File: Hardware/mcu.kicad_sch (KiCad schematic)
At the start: 10 parts, among them Q1 BSS138DW-7-F, U6 AS7341-DLGT

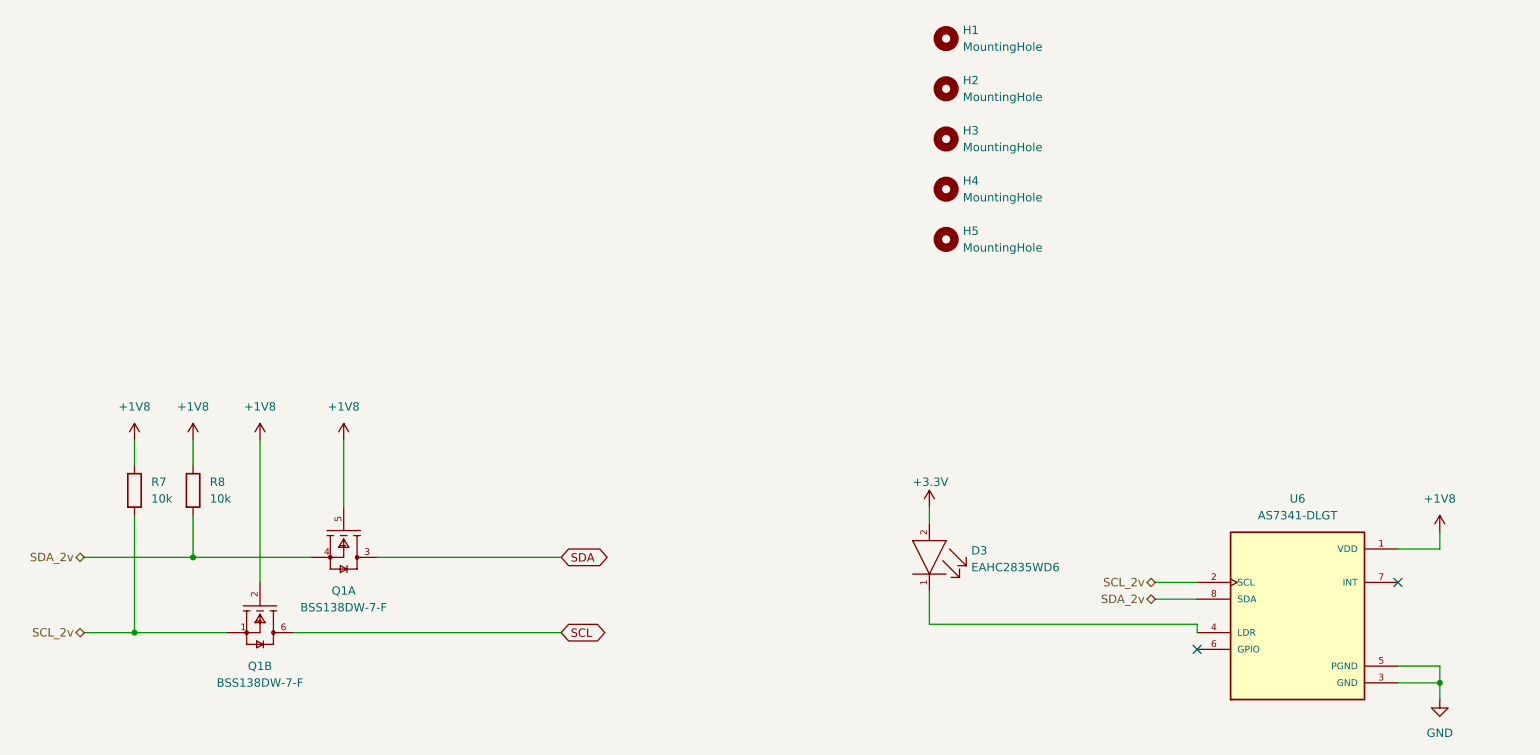
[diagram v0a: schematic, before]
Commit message: Version 0.6 - 4 layer version
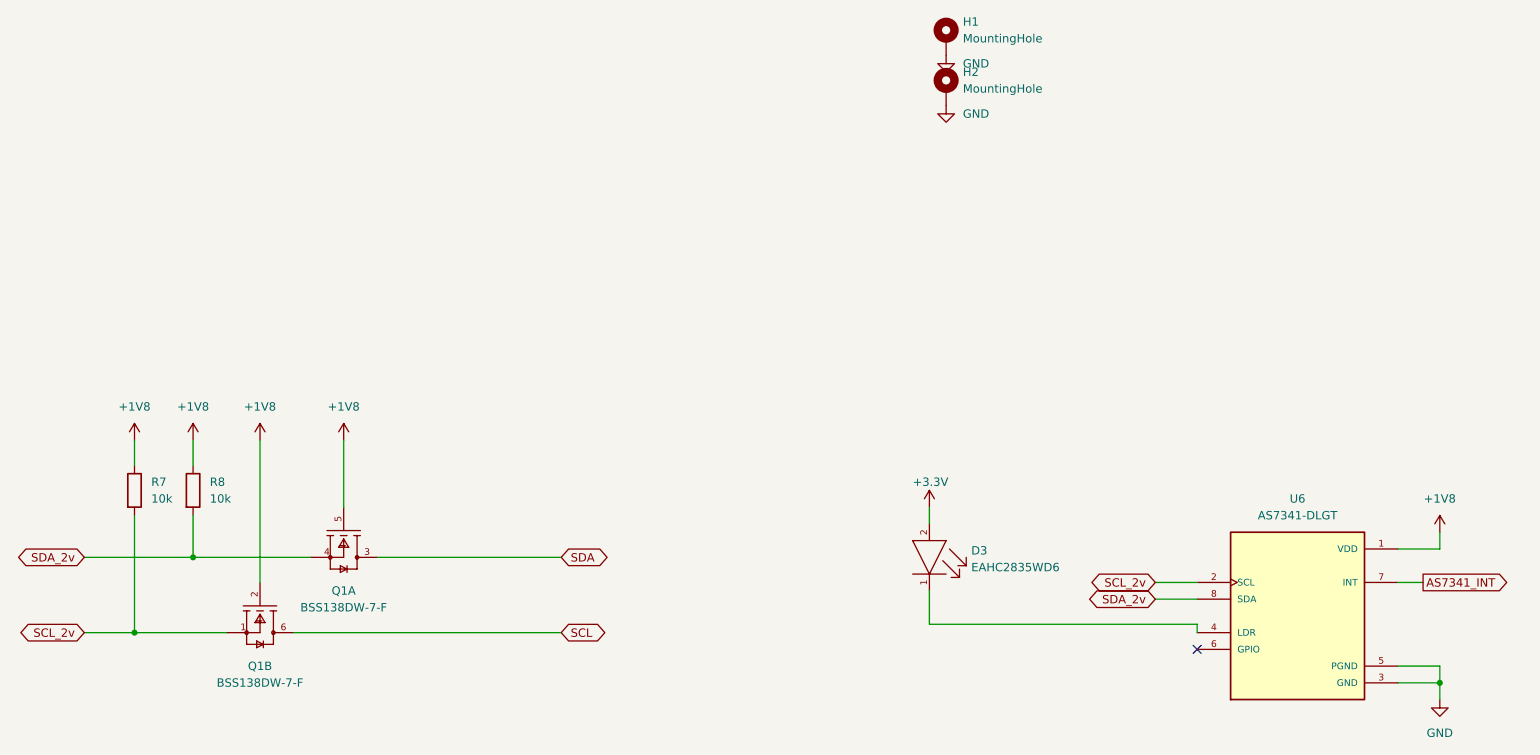
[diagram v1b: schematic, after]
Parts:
- removed H3, H4, H5: MountingHole, MountingHole:MountingHole_2.2mm_M2_ISO7380_Pad, symbol Mechanical:MountingHole
- H1, H2: symbol Mechanical:MountingHole -> Mechanical:MountingHole_Pad
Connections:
- net GND: now also H1.1, H2.1
- net AS7341_INT: now reaches U6.7 (INT)
- no-connect marks 2 -> 1
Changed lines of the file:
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@@
   (junction (at 68.58 110.49) (diameter 0) (color 0 0 0 0)
   )
-  (no_connect (at 251.46 114.3))
   (no_connect (at 220.98 124.46))
   (wire (pts (xy 180.34 102.87) (xy 180.34 105.41))
@@
     (stroke (width 0) (type default) (color 0 0 0 0))
   )
+  (wire (pts (xy 251.46 114.3) (xy 255.27 114.3))
+    (stroke (width 0) (type default) (color 0 0 0 0))
+  )
   (wire (pts (xy 68.58 104.14) (xy 68.58 110.49))
     (stroke (width 0) (type default) (color 0 0 0 0))
@@
   (wire (pts (xy 59.69 121.92) (xy 73.66 121.92))
     (stroke (width 0) (type default) (color 0 0 0 0))
+  )
+  (global_label "SCL_2v" (shape bidirectional) (at 52.07 121.92 180) (fields_autoplaced)
+    (effects (font (size 1.27 1.27)) (justify right))
+    (property "Intersheet References" "${INTERSHEET_REFS}" (id 0) (at 43.0045 121.8406 0)
+      (effects (font (size 1.27 1.27)) (justify right) hide)
+    )
+  )
+  (global_label "SDA_2v" (shape bidirectional) (at 214.63 116.84 180) (fields_autoplaced)
+    (effects (font (size 1.27 1.27)) (justify right))
+    (property "Intersheet References" "${INTERSHEET_REFS}" (id 0) (at 205.504 116.7606 0)
+      (effects (font (size 1.27 1.27)) (justify right) hide)
+    )
   )
   (global_label "SDA" (shape bidirectional) (at 124.46 110.49 0) (fields_autoplaced)
@@
     )
   )
+  (global_label "SDA_2v" (shape bidirectional) (at 52.07 110.49 180) (fields_autoplaced)
+    (effects (font (size 1.27 1.27)) (justify right))
+    (property "Intersheet References" "${INTERSHEET_REFS}" (id 0) (at 42.944 110.4106 0)
+      (effects (font (size 1.27 1.27)) (justify right) hide)
+    )
+  )
+  (global_label "SCL_2v" (shape bidirectional) (at 214.63 114.3 180) (fields_autoplaced)
+    (effects (font (size 1.27 1.27)) (justify right))
+    (property "Intersheet References" "${INTERSHEET_REFS}" (id 0) (at 205.5645 114.2206 0)
+      (effects (font (size 1.27 1.27)) (justify right) hide)
+    )
+  )
+  (global_label "AS7341_INT" (shape output) (at 255.27 114.3 0) (fields_autoplaced)
+    (effects (font (size 1.27 1.27)) (justify left))
+    (property "Intersheet References" "${INTERSHEET_REFS}" (id 0) (at 268.6898 114.2206 0)
+      (effects (font (size 1.27 1.27)) (justify left) hide)
+    )
+  )
   (global_label "SCL" (shape bidirectional) (at 124.46 121.92 0) (fields_autoplaced)
     (effects (font (size 1.27 1.27)) (justify left))
@@
     )
   )
-  (hierarchical_label "SCL_2v" (shape bidirectional) (at 52.07 121.92 180)
-    (effects (font (size 1.27 1.27)) (justify right))
-  )
-  (hierarchical_label "SDA_2v" (shape bidirectional) (at 52.07 110.49 180)
-    (effects (font (size 1.27 1.27)) (justify right))
-  )
-  (hierarchical_label "SDA_2v" (shape bidirectional) (at 214.63 116.84 180)
-    (effects (font (size 1.27 1.27)) (justify right))
-  )
-  (hierarchical_label "SCL_2v" (shape bidirectional) (at 214.63 114.3 180)
-    (effects (font (size 1.27 1.27)) (justify right))
-  )
   (symbol (lib_id "Device:R") (at 68.58 100.33 0) (unit 1)
     (in_bom yes) (on_board yes) (fields_autoplaced)
@@
     (pin "2")
   )
-  (symbol (lib_id "Mechanical:MountingHole") (at 182.88 39.37 0) (unit 1)
-    (in_bom yes) (on_board yes) (fields_autoplaced)
-    (property "Reference" "H2" (id 0) (at 185.42 38.0999 0)
-      (effects (font (size 1.27 1.27)) (justify left))
-    )
-    (property "Value" "MountingHole" (id 1) (at 185.42 40.6399 0)
+  (symbol (lib_id "power:GND") (at 182.88 34.29 0) (unit 1)
+    (in_bom yes) (on_board yes) (fields_autoplaced)
+    (property "Reference" "#PWR0112" (id 0) (at 182.88 40.64 0)
+      (effects (font (size 1.27 1.27)) hide)
+    )
+    (property "Value" "GND" (id 1) (at 185.42 35.5599 0)
+      (effects (font (size 1.27 1.27)) (justify left))
+    )
+    (property "Footprint" "" (id 2) (at 182.88 34.29 0)
+      (effects (font (size 1.27 1.27)) hide)
+    )
+    (property "Datasheet" "" (id 3) (at 182.88 34.29 0)
+      (effects (font (size 1.27 1.27)) hide)
+    )
+    (pin "1")
+  )
+  (symbol (lib_id "Mechanical:MountingHole_Pad") (at 182.88 39.37 0) (unit 1)
+    (in_bom yes) (on_board yes) (fields_autoplaced)
+    (property "Reference" "H2" (id 0) (at 185.42 36.8299 0)
+      (effects (font (size 1.27 1.27)) (justify left))
+    )
+    (property "Value" "MountingHole" (id 1) (at 185.42 39.3699 0)
       (effects (font (size 1.27 1.27)) (justify left))
     )
@@
       (effects (font (size 1.27 1.27)) hide)
     )
+    (pin "1")
   )
   (symbol (lib_id "Everlight-EAHC2835WD6:EAHC2835WD6") (at 180.34 102.87 270) (unit 1)
@@
     (pin "1")
     (pin "2")
-  )
-  (symbol (lib_id "Mechanical:MountingHole") (at 182.88 62.23 0) (unit 1)
-    (in_bom yes) (on_board yes) (fields_autoplaced)
-    (property "Reference" "H5" (id 0) (at 185.42 60.9599 0)
-      (effects (font (size 1.27 1.27)) (justify left))
-    )
-    (property "Value" "MountingHole" (id 1) (at 185.42 63.4999 0)
-      (effects (font (size 1.27 1.27)) (justify left))
-    )
-    (property "Footprint" "MountingHole:MountingHole_2.2mm_M2_ISO7380_Pad" (id 2) (at 182.88 62.23 0)
-      (effects (font (size 1.27 1.27)) hide)
-    )
-    (property "Datasheet" "~" (id 3) (at 182.88 62.23 0)
-      (effects (font (size 1.27 1.27)) hide)
-    )
   )
   (symbol (lib_id "power:+3.3V") (at 180.34 102.87 0) (unit 1)
@@
     (pin "1")
   )
-  (symbol (lib_id "Mechanical:MountingHole") (at 182.88 46.99 0) (unit 1)
-    (in_bom yes) (on_board yes) (fields_autoplaced)
-    (property "Reference" "H3" (id 0) (at 185.42 45.7199 0)
-      (effects (font (size 1.27 1.27)) (justify left))
-    )
-    (property "Value" "MountingHole" (id 1) (at 185.42 48.2599 0)
-      (effects (font (size 1.27 1.27)) (justify left))
-    )
-    (property "Footprint" "MountingHole:MountingHole_2.2mm_M2_ISO7380_Pad" (id 2) (at 182.88 46.99 0)
-      (effects (font (size 1.27 1.27)) hide)
-    )
-    (property "Datasheet" "~" (id 3) (at 182.88 46.99 0)
-      (effects (font (size 1.27 1.27)) hide)
-    )
-  )
   (symbol (lib_id "Diodes_Inc._-_BSS138DW-7-F:BSS138DW-7-F") (at 91.44 100.33 270) (unit 1)
     (in_bom yes) (on_board yes) (fields_autoplaced)
@@
     (pin "1")
     (pin "2")
-  )
-  (symbol (lib_id "Mechanical:MountingHole") (at 182.88 54.61 0) (unit 1)
-    (in_bom yes) (on_board yes) (fields_autoplaced)
-    (property "Reference" "H4" (id 0) (at 185.42 53.3399 0)
-      (effects (font (size 1.27 1.27)) (justify left))
-    )
-    (property "Value" "MountingHole" (id 1) (at 185.42 55.8799 0)
-      (effects (font (size 1.27 1.27)) (justify left))
-    )
-    (property "Footprint" "MountingHole:MountingHole_2.2mm_M2_ISO7380_Pad" (id 2) (at 182.88 54.61 0)
-      (effects (font (size 1.27 1.27)) hide)
-    )
-    (property "Datasheet" "~" (id 3) (at 182.88 54.61 0)
-      (effects (font (size 1.27 1.27)) hide)
-    )
   )
   (symbol (lib_id "AS7341-DLGT:AS7341-DLGT") (at 236.22 119.38 0) (unit 1)
@@
     (pin "8")
   )
-  (symbol (lib_id "Mechanical:MountingHole") (at 182.88 31.75 0) (unit 1)
-    (in_bom yes) (on_board yes) (fields_autoplaced)
-    (property "Reference" "H1" (id 0) (at 185.42 30.4799 0)
-      (effects (font (size 1.27 1.27)) (justify left))
-    )
-    (property "Value" "MountingHole" (id 1) (at 185.42 33.0199 0)
+  (symbol (lib_id "Mechanical:MountingHole_Pad") (at 182.88 31.75 0) (unit 1)
+    (in_bom yes) (on_board yes) (fields_autoplaced)
+    (property "Reference" "H1" (id 0) (at 185.42 29.2099 0)
+      (effects (font (size 1.27 1.27)) (justify left))
+    )
+    (property "Value" "MountingHole" (id 1) (at 185.42 31.7499 0)
       (effects (font (size 1.27 1.27)) (justify left))
     )
@@
       (effects (font (size 1.27 1.27)) hide)
     )
+    (pin "1")
   )
   (symbol (lib_id "power:+1V8") (at 257.81 106.68 0) (unit 1)
@@
       (effects (font (size 1.27 1.27)) hide)
     )
+    (pin "1")
+  )
+  (symbol (lib_id "power:GND") (at 182.88 41.91 0) (unit 1)
+    (in_bom yes) (on_board yes) (fields_autoplaced)
+    (property "Reference" "#PWR0108" (id 0) (at 182.88 48.26 0)
+      (effects (font (size 1.27 1.27)) hide)
+    )
+    (property "Value" "GND" (id 1) (at 185.42 43.1799 0)
+      (effects (font (size 1.27 1.27)) (justify left))
+    )
+    (property "Footprint" "" (id 2) (at 182.88 41.91 0)
+      (effects (font (size 1.27 1.27)) hide)
+    )
+    (property "Datasheet" "" (id 3) (at 182.88 41.91 0)
+      (effects (font (size 1.27 1.27)) hide)
+    )
